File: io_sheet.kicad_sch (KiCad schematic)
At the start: 0 parts

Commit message: Comecei a adicionar a parte das entradas e continuo mexendo na parte do STM32
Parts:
- added J2: Conn_02x06_Counter_Clockwise, BajaKICAD:MX120G, symbol Connector_Generic:Conn_02x06_Counter_Clockwise
- added R10, R11, R14, R16, R17, R19, R6, R7: 10K, Resistor_SMD:R_1206_3216Metric, symbol Device:R
- added R12, R13, R15, R18, R4, R5, R8, R9: 680, Resistor_SMD:R_1206_3216Metric, symbol Device:R
- added R20, R21, R22, R23: 1k, symbol Device:R
- added RV1, RV2, RV3, RV4: 10k_trim, symbol Device:R_Potentiometer_Trim
- added U10, U2, U3, U4, U5, U6, U7, U8: PC817, Package_DIP:DIP-4_W7.62mm_SMDSocket_SmallPads, symbol Isolator:PC817
- added U9: LM324, symbol Amplifier_Operational:LM324
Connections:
- new net: R9.2, U4.1
- new net: R10.2, U4.4
- new net: R6.2, U3.4
- new net: R13.2, U6.1
- new net: R16.2, U6.4
- new net: R18.2, U7.1
- new net: R19.2, U7.4
- new net: R7.2, U2.4
- new net: R22.1, U9.8
- new net: R22.2, RV3.3
- new net: R20.1, U9.1
- new net: RV1.2, U9.2 (-)
- new net: R8.2, U5.1
- new net: R11.2, U5.4
- new net: R12.2, U8.1
- new net: R14.2, U8.4
- new net: R5.2, U3.1
- new net: R20.2, RV1.3
- new net: R15.2, U10.1
- new net: RV4.2, U9.13 (-)
- new net: R23.1, U9.14
- new net: R21.1, U9.7
- new net: R21.2, RV2.3
- new net: RV3.2, U9.9 (-)
- new net: R17.2, U10.4
- new net: RV2.2, U9.6 (-)
- new net: R23.2, RV4.3
- new net: R4.2, U2.1
- new net 3V3: R10.1, R11.1, R14.1, R16.1, R17.1, R19.1, R6.1, R7.1
- new net AN3V3: U9.4 (V+)
- new net AN_IN_0: J2.9 (Pin_9), U9.3 (+)
- new net AN_IN_1: J2.10 (Pin_10), U9.5 (+)
- new net AN_IN_2: J2.11 (Pin_11), U9.10 (+)
- new net AN_IN_3: J2.12 (Pin_12), U9.12 (+)
- new net DG_IN_0: J2.1 (Pin_1), R4.1
- new net DG_IN_1: J2.2 (Pin_2), R8.1
- new net DG_IN_2: J2.3 (Pin_3), R12.1
- new net DG_IN_3: J2.4 (Pin_4), R15.1
- new net DG_IN_4: J2.5 (Pin_5), R5.1
- new net DG_IN_5: J2.6 (Pin_6), R9.1
- new net DG_IN_6: J2.7 (Pin_7), R13.1
- new net DG_IN_7: J2.8 (Pin_8), R18.1
- new net GNDA: RV1.1, RV2.1, RV3.1, RV4.1, U10.2, U2.2, U3.2, U4.2, U5.2, U6.2, U7.2, U8.2, U9.11 (V-)
- new net GNDD: U10.3, U2.3, U3.3, U4.3, U5.3, U6.3, U7.3, U8.3
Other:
- note added: "Conector Molex"
- note added: "Entradas Analógicas"
- note added: "Entradas Opto-Acopladas"
- note added: "Nota: Ganho até de 1/10 regulável ( Rtrim = 10k e Ramp = 1k)"

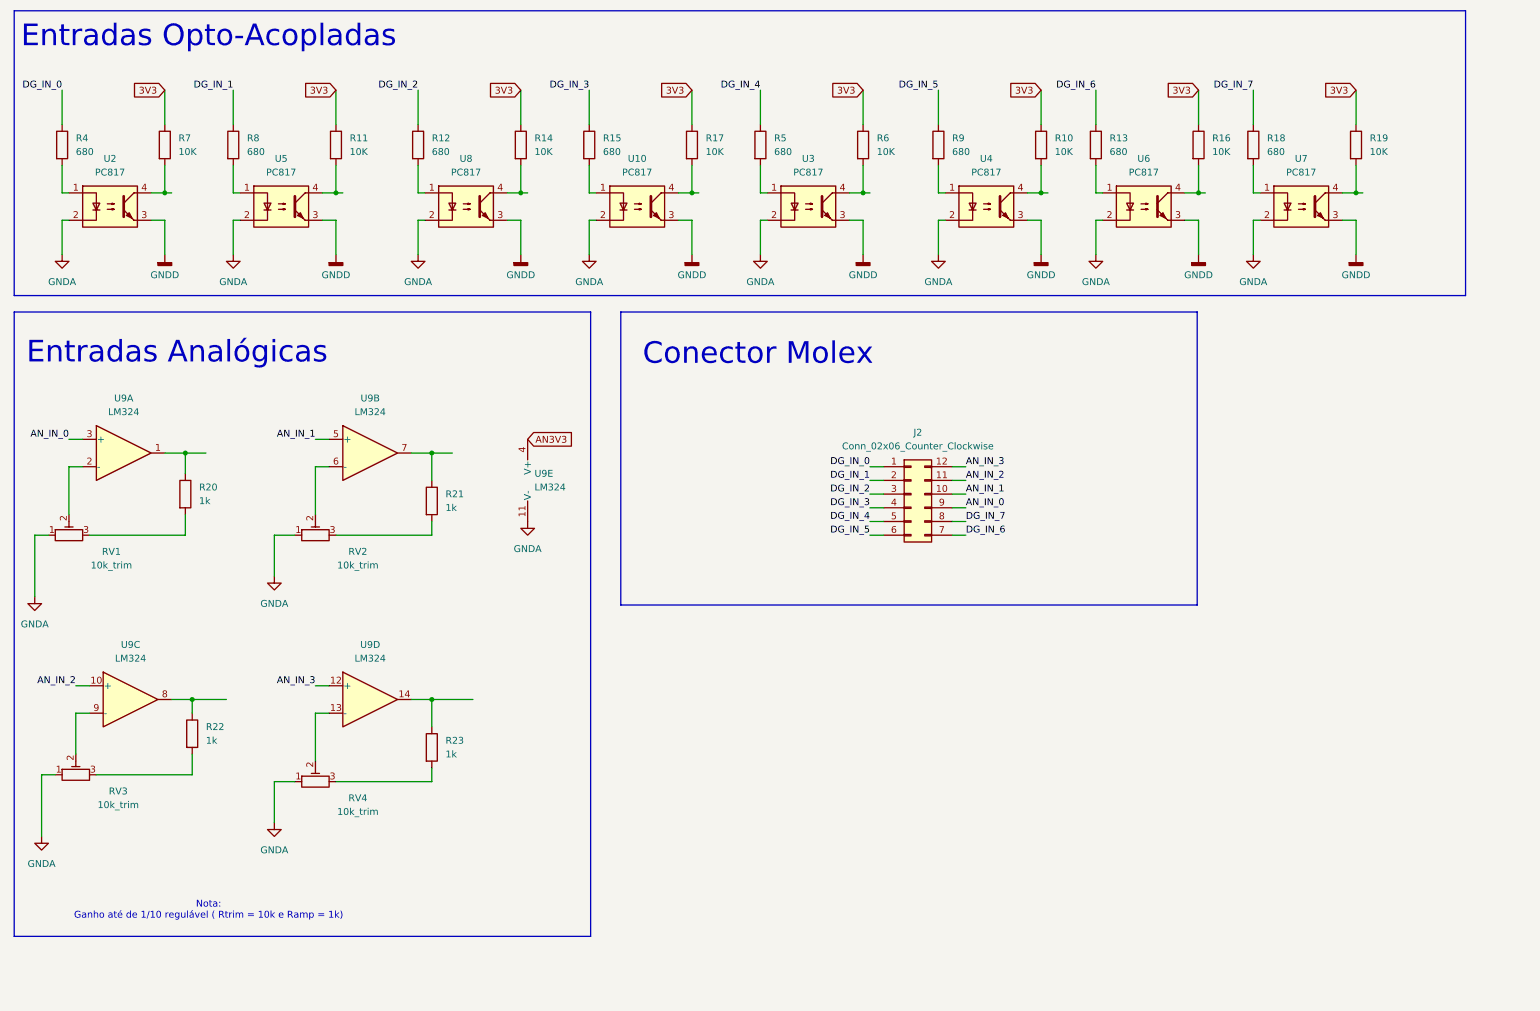
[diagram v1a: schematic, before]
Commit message: Troquei o micro para STM32H523, adicionei o cristal HSE, circuito da fonte de 5V e 3v3, CAN, SD
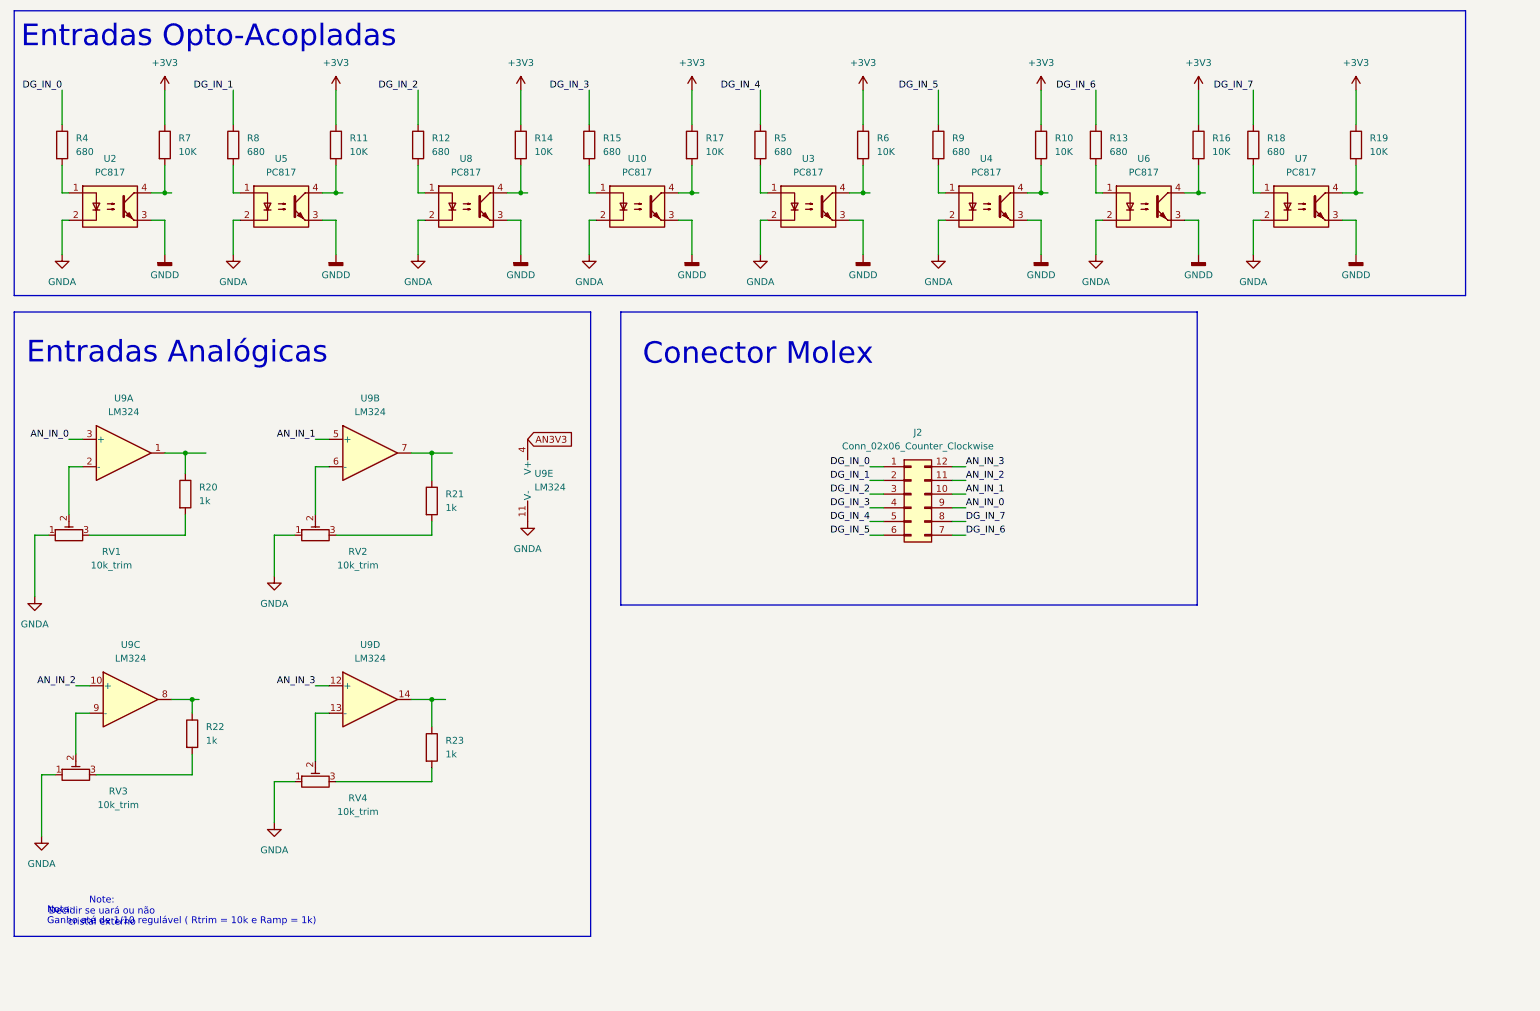
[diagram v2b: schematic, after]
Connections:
- net 3V3 renamed +3V3
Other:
- note added: "Note: Decidir se uará ou não cristal externo"

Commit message: Alterei o nome para o par diferencial do CAN, adicionei capacitores de desacoplamento para todas as alimentacoes
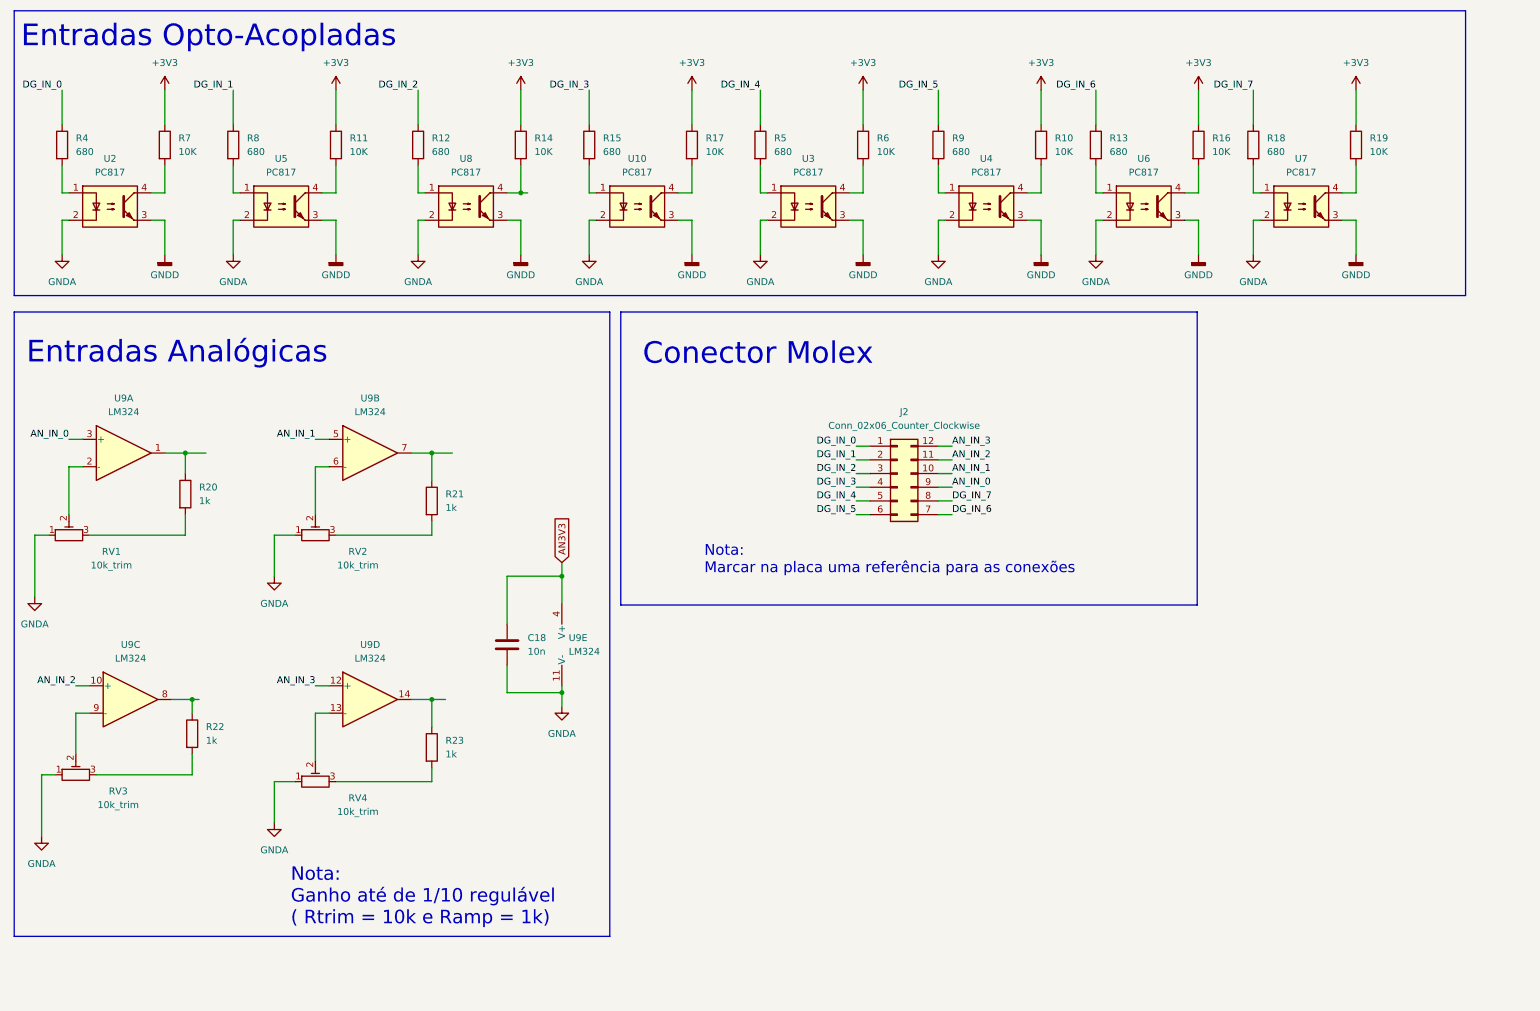
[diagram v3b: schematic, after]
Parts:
- added C18: 10n, symbol Device:C
- R20, R21, R22, R23: footprint (none) -> LED_SMD:LED_1206_3216Metric_Pad1.42x1.75mm_HandSolder
- RV1, RV2, RV3, RV4: footprint (none) -> Potentiometer_THT:Potentiometer_Bourns_3296W_Vertical
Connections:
- net AN3V3: now also C18.1
- net GNDA: now also C18.2
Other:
- note added: "Nota: Marcar na placa uma referência para as conexões"
- note removed: "Note: Decidir se uará ou não cristal externo"
- moved on the sheet: J2, U9E

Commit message: Removi as entradas analógicas, projeto delas estava errado
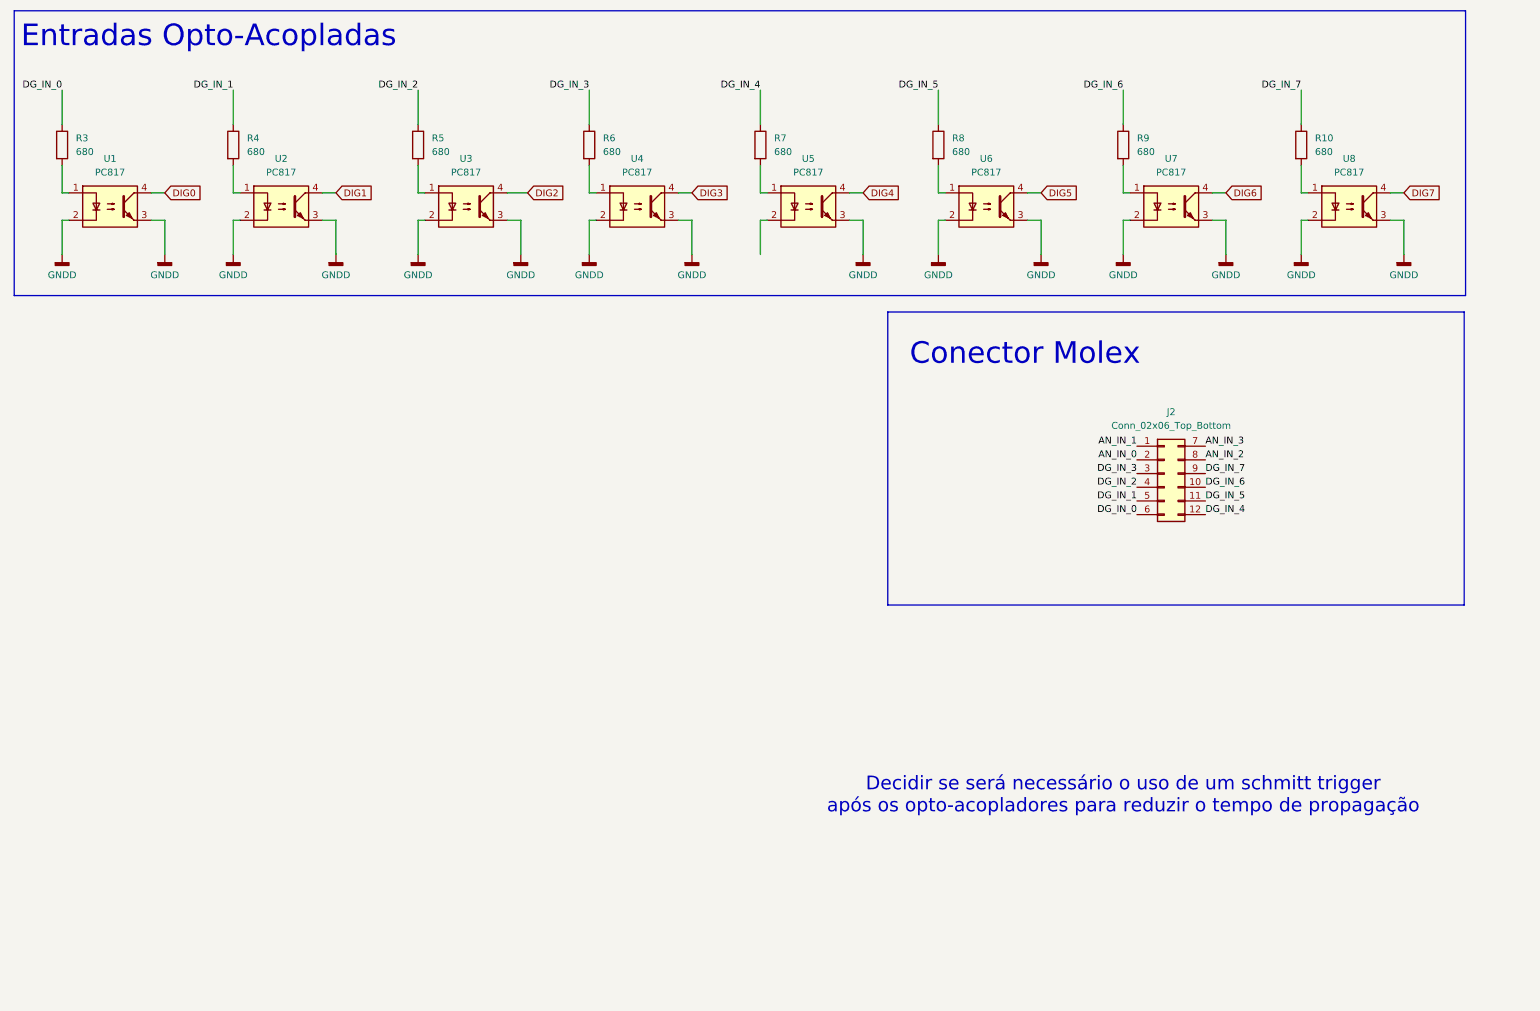
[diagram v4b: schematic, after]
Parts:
- removed C18: 10n, symbol Device:C
- removed J2: Conn_02x06_Counter_Clockwise, BajaKICAD:MX120G, symbol Connector_Generic:Conn_02x06_Counter_Clockwise
- removed R10, R11, R14, R16, R17, R19, R6, R7: 10K, Resistor_SMD:R_1206_3216Metric, symbol Device:R
- removed R20, R21, R22, R23: 1k, LED_SMD:LED_1206_3216Metric_Pad1.42x1.75mm_HandSolder, symbol Device:R
- removed RV1, RV2, RV3, RV4: 10k_trim, Potentiometer_THT:Potentiometer_Bourns_3296W_Vertical, symbol Device:R_Potentiometer_Trim
- removed U9: LM324, symbol Amplifier_Operational:LM324
- added J2: Conn_02x06_Top_Bottom, Baja_Library:MX120G, symbol Connector_Generic:Conn_02x06_Top_Bottom
- R10: renamed from R18; footprint Resistor_SMD:R_1206_3216Metric -> Resistor_SMD:R_1206_3216Metric_Pad1.30x1.75mm_HandSolder
- R3: renamed from R4; footprint Resistor_SMD:R_1206_3216Metric -> Resistor_SMD:R_1206_3216Metric_Pad1.30x1.75mm_HandSolder
- R4: renamed from R8; footprint Resistor_SMD:R_1206_3216Metric -> Resistor_SMD:R_1206_3216Metric_Pad1.30x1.75mm_HandSolder
- R5: renamed from R12; footprint Resistor_SMD:R_1206_3216Metric -> Resistor_SMD:R_1206_3216Metric_Pad1.30x1.75mm_HandSolder
- R6: renamed from R15; footprint Resistor_SMD:R_1206_3216Metric -> Resistor_SMD:R_1206_3216Metric_Pad1.30x1.75mm_HandSolder
- R7: renamed from R5; footprint Resistor_SMD:R_1206_3216Metric -> Resistor_SMD:R_1206_3216Metric_Pad1.30x1.75mm_HandSolder
- R8: renamed from R9; footprint Resistor_SMD:R_1206_3216Metric -> Resistor_SMD:R_1206_3216Metric_Pad1.30x1.75mm_HandSolder
- R9: renamed from R13; footprint Resistor_SMD:R_1206_3216Metric -> Resistor_SMD:R_1206_3216Metric_Pad1.30x1.75mm_HandSolder
- U8: renamed from U7; footprint Package_DIP:DIP-4_W7.62mm_SMDSocket_SmallPads -> Baja_Library:SO-4_HandSoldering
- renumbered U2 to U1, U5 to U2, U8 to U3, U10 to U4, U3 to U5, U4 to U6, U6 to U7
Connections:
- net AN_IN_0: now also J2.2 (Pin_2)
- net AN_IN_1: now also J2.1 (Pin_1)
- net AN_IN_2: now also J2.8 (Pin_8)
- net AN_IN_3: now also J2.7 (Pin_7)
- net DG_IN_0: now also J2.6 (Pin_6)
- net DG_IN_1: now also J2.5 (Pin_5)
- net DG_IN_2: now also J2.4 (Pin_4)
- net DG_IN_3: now also J2.3 (Pin_3)
- net DG_IN_4: now also J2.12 (Pin_12)
- net DG_IN_5: now also J2.11 (Pin_11)
- net DG_IN_6: now also J2.10 (Pin_10)
- net DG_IN_7: now also J2.9 (Pin_9)
- net GNDD: now also U1.2, U2.2, U3.2, U4.2, U6.2, U7.2, U8.2
- net DIG5: now reaches U6.4
- net DIG4: now reaches U5.4
- net DIG6: now reaches U7.4
- net DIG7: now reaches U8.4
- net DIG0: now reaches U1.4
- net DIG1: now reaches U2.4
- net DIG2: now reaches U3.4
- net DIG3: now reaches U4.4
- removed net GNDA: U1.2, U2.2, U3.2, U4.2, U5.2, U6.2, U7.2, U8.2
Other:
- note added: "Decidir se será necessário o uso de um schmitt trigger após os opto-acopladores para reduzir o tempo de propagação"
- note removed: "Entradas Analógicas"
- note removed: "Nota: Ganho até de 1/10 regulável ( Rtrim = 10k e Ramp = 1k)"
- note removed: "Nota: Marcar na placa uma referência para as conexões"
- moved on the sheet: R10, R9, U7, U8
